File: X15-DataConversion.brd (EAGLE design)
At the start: 24.3 x 25.4 mm, 24 parts, among them Y1 ECS-80-18-30-JGN-TR

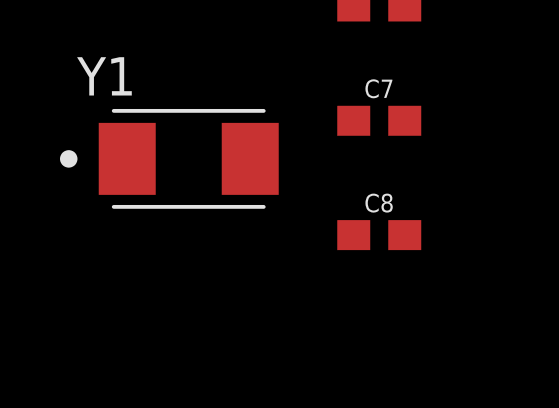
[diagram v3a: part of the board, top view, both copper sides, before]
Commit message: oscillator resistor and capacitor labels
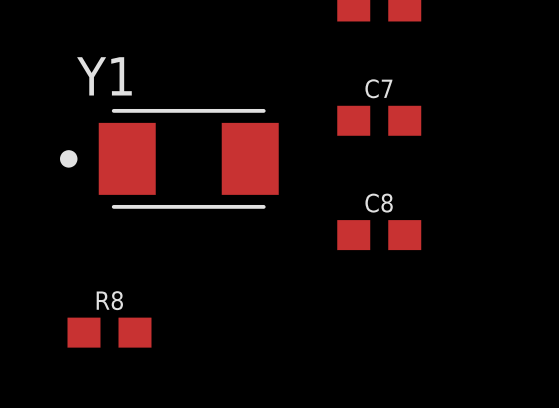
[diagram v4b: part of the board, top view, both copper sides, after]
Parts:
- added R8: 0, SparkFun-Resistors:0603
- R9: value 1.5k -> 0
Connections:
- net OSC_IN: now also R8.1, R8.2
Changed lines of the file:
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@@
 <attribute name="VALUE" x="-36.83" y="-83.312" size="0.6096" layer="27" font="vector" ratio="20" align="top-center"/>
 </element>
-<element name="R9" library="SparkFun-Resistors" package="0603" value="1.5k" x="-36.83" y="-110.49" smashed="yes">
+<element name="R9" library="SparkFun-Resistors" package="0603" value="0" x="-36.83" y="-110.49" smashed="yes">
 <attribute name="NAME" x="-36.83" y="-109.728" size="0.6096" layer="25" font="vector" ratio="20" align="bottom-center"/>
 <attribute name="PROD_ID" value=" " x="-35.56" y="-110.49" size="1.778" layer="27" display="off"/>
@@
 <attribute name="PURCHASE-URL" value="https://pricing.snapeda.com/search/part/ECS-80-18-30-JGN-TR/?ref=eda" x="-43.18" y="-115.57" size="1.778" layer="27" display="off"/>
 <attribute name="VALUE" x="-46.89308125" y="-119.0322" size="1.274490625" layer="27"/>
+</element>
+<element name="R8" library="SparkFun-Resistors" package="0603" value="0" x="-45.8216" y="-121.3612" smashed="yes">
+<attribute name="NAME" x="-45.8216" y="-120.5992" size="0.6096" layer="25" font="vector" ratio="20" align="bottom-center"/>
+<attribute name="PROD_ID" value=" " x="-45.6946" y="-121.3612" size="1.778" layer="27" display="off"/>
+<attribute name="VALUE" x="-45.8216" y="-122.1232" size="0.6096" layer="27" font="vector" ratio="20" align="top-center"/>
 </element>
 </elements>
@@
 <contactref element="C7" pad="1"/>
 <contactref element="Y1" pad="1"/>
+<contactref element="R8" pad="1"/>
+<contactref element="R8" pad="2"/>
+<wire x1="-44.9716" y1="-121.3612" x2="-46.6716" y2="-121.3612" width="0" layer="19" extent="1-1"/>
+<wire x1="-45.23" y1="-115.57" x2="-44.9716" y2="-121.3612" width="0" layer="19" extent="1-1"/>
 <wire x1="-37.68" y1="-114.3" x2="-45.23" y2="-115.57" width="0" layer="19" extent="1-1"/>
 <wire x1="-8.5" y1="-48.36" x2="-37.68" y2="-114.3" width="0" layer="19" extent="1-1"/>

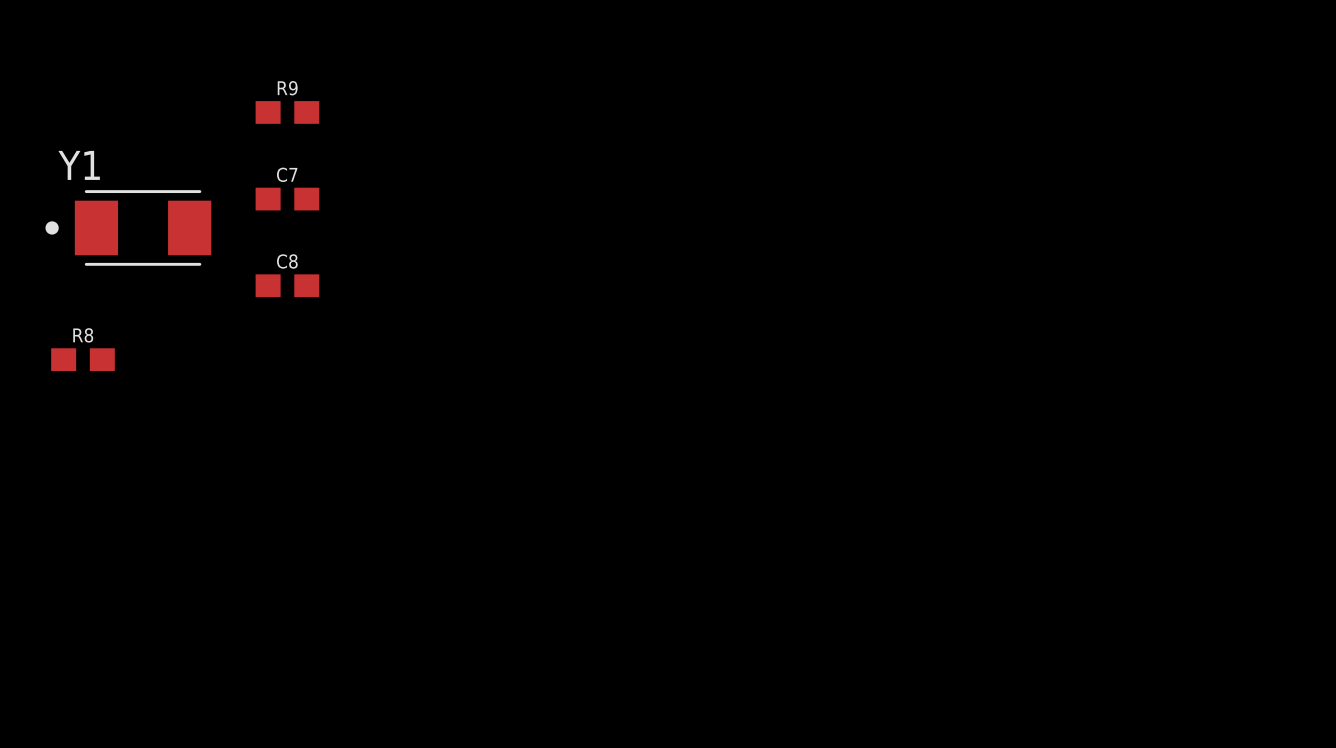
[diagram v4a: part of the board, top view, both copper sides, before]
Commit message: replaced oscillator with same one as on Pi Shield
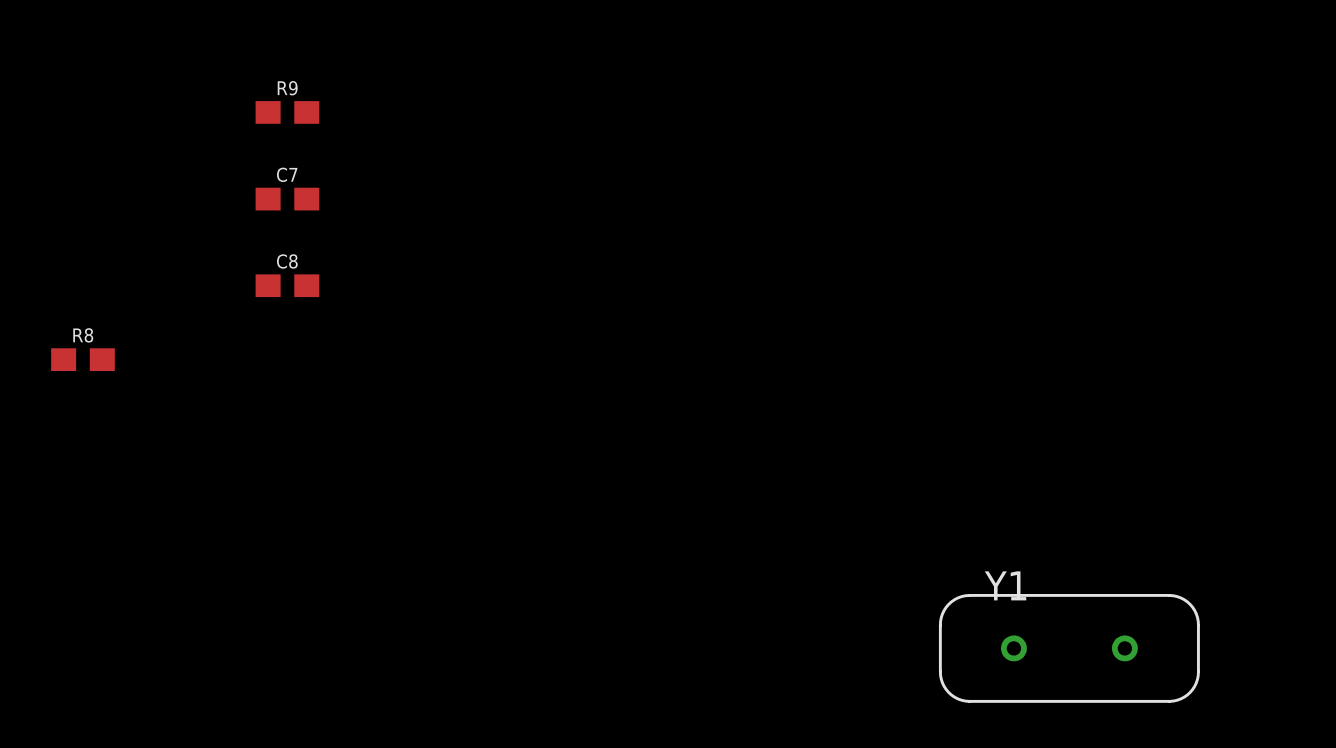
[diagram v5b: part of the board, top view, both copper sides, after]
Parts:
- Y1: value ECS-80-18-30-JGN-TR -> ECS-80-18-4X; device ECS-80-18-30-JGN-TR:XTAL_ECS-80-18-30-JGN-TR -> ECS-80-18-4X:XTAL_ECS-80-18-4X
- moved Y1 44.7 mm to (-2.44, -134.1)
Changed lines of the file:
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@@
 <setting verticaltext="up"/>
 </settings>
-<grid distance="1" unitdist="mil" unit="mil" style="lines" multiple="1" display="no" altdistance="5" altunitdist="mil" altunit="mil"/>
+<grid distance="2" unitdist="mm" unit="mm" style="lines" multiple="1" display="yes" altdistance="5" altunitdist="mil" altunit="mil"/>
 <layers>
 <layer number="1" name="Top" color="4" fill="1" visible="yes" active="yes"/>
@@
 <attribute name="VALUE" x="-36.83" y="-118.872" size="0.6096" layer="27" font="vector" ratio="20" align="top-center"/>
 </element>
-<element name="Y1" library="ECS-80-18-30-JGN-TR" package="XTAL_ECS-80-18-30-JGN-TR" value="ECS-80-18-30-JGN-TR" x="-43.18" y="-115.57" smashed="yes">
-<attribute name="DESCRIPTION" value=" 8 MHz ±20ppm Crystal 18pF 100 Ohms 2-SMD, No Lead " x="-43.18" y="-115.57" size="1.778" layer="27" display="off"/>
-<attribute name="DIGI-KEY_PART_NUMBER" value="XC2103TR-ND" x="-43.18" y="-115.57" size="1.778" layer="27" display="off"/>
-<attribute name="MF" value="ECS Inc." x="-43.18" y="-115.57" size="1.778" layer="27" display="off"/>
-<attribute name="MP" value="ECS-80-18-30-JGN-TR" x="-43.18" y="-115.57" size="1.778" layer="27" display="off"/>
-<attribute name="NAME" x="-46.89928125" y="-113.45771875" size="1.27743125" layer="25"/>
-<attribute name="PACKAGE" value="SMD-2 ECS International" x="-43.18" y="-115.57" size="1.778" layer="27" display="off"/>
-<attribute name="PURCHASE-URL" value="https://pricing.snapeda.com/search/part/ECS-80-18-30-JGN-TR/?ref=eda" x="-43.18" y="-115.57" size="1.778" layer="27" display="off"/>
-<attribute name="VALUE" x="-46.89308125" y="-119.0322" size="1.274490625" layer="27"/>
+<element name="Y1" library="ECS-80-18-4X" package="XTAL_ECS-80-18-4X" value="ECS-80-18-4X" x="-2.44" y="-134.0612" smashed="yes">
+<attribute name="DESCRIPTION" value=" 8 MHz ±30ppm Crystal 18pF 80 Ohms HC-49/US " x="-2.44" y="-134.0612" size="1.778" layer="27" display="off"/>
+<attribute name="DIGI-KEY_PART_NUMBER" value="X1093-ND" x="-2.44" y="-134.0612" size="1.778" layer="27" display="off"/>
+<attribute name="MF" value="ECS Inc." x="-2.44" y="-134.0612" size="1.778" layer="27" display="off"/>
+<attribute name="MP" value="ECS-80-18-4X" x="-2.44" y="-134.0612" size="1.778" layer="27" display="off"/>
+<attribute name="NAME" x="-6.15928125" y="-131.94891875" size="1.27743125" layer="25"/>
+<attribute name="PACKAGE" value="HC-49US ECS Inc." x="-2.44" y="-134.0612" size="1.778" layer="27" display="off"/>
+<attribute name="PURCHASE-URL" value="https://pricing.snapeda.com/search/part/ECS-80-18-4X/?ref=eda" x="-2.44" y="-134.0612" size="1.778" layer="27" display="off"/>
+<attribute name="VALUE" x="-6.15308125" y="-137.5234" size="1.274490625" layer="27"/>
 </element>
 <element name="R8" library="SparkFun-Resistors" package="0603" value="0" x="-45.8216" y="-121.3612" smashed="yes">
@@
 <contactref element="R8" pad="2"/>
 <wire x1="-44.9716" y1="-121.3612" x2="-46.6716" y2="-121.3612" width="0" layer="19" extent="1-1"/>
-<wire x1="-45.23" y1="-115.57" x2="-44.9716" y2="-121.3612" width="0" layer="19" extent="1-1"/>
-<wire x1="-37.68" y1="-114.3" x2="-45.23" y2="-115.57" width="0" layer="19" extent="1-1"/>
+<wire x1="-37.68" y1="-114.3" x2="-44.9716" y2="-121.3612" width="0" layer="19" extent="1-1"/>
+<wire x1="-4.88" y1="-134.0612" x2="-37.68" y2="-114.3" width="0" layer="19" extent="1-1"/>
 <wire x1="-8.5" y1="-48.36" x2="-37.68" y2="-114.3" width="0" layer="19" extent="1-1"/>
 </signal>
@@
 <contactref element="R9" pad="1"/>
 <contactref element="Y1" pad="2"/>
-<wire x1="-37.68" y1="-118.11" x2="-41.13" y2="-115.57" width="0" layer="19" extent="1-1"/>
-<wire x1="-37.68" y1="-110.49" x2="-41.13" y2="-115.57" width="0" layer="19" extent="1-1"/>
+<wire x1="-37.68" y1="-110.49" x2="-37.68" y2="-118.11" width="0" layer="19" extent="1-1"/>
+<wire x1="0" y1="-134.0612" x2="-37.68" y2="-118.11" width="0" layer="19" extent="1-1"/>
 </signal>
 </signals>

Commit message: starting layout
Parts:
- moved U$1 79.8 mm to (8.13, 22.2)
- moved STM 68.8 mm to (10.3, 11.9), turned to 90 degrees

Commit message: starting wiring
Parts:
- Y1: device ECS-80-18-4X:XTAL_ECS-80-18-4X -> OTHER, ECS-80-18-4X:XTAL_ECS-80-18-4X
- moved R8 147.8 mm to (6.80, 16.8)
- moved Y1 144.0 mm to (4.06, 9.81), turned to 90 degrees
- moved R9 136.1 mm to (6.79, 18.4)
- moved C8 133.3 mm to (8.54, 7.26)
- moved C7 127.9 mm to (8.54, 5.33)
- moved CAN_TRANCEIVER 119.7 mm to (18.6, 18.3), turned to 90 degrees
- moved R7 117.3 mm to (20.5, 19.8), flipped to the bottom
- moved R6 115.4 mm to (20.6, 21.4), flipped to the bottom
- moved C6 104.8 mm to (21.9, 11.8)
- moved D3 82.2 mm to (21.8, 7.92), turned to 180 degrees
- moved R5 77.3 mm to (21.8, 10.0), turned to 180 degrees
- moved CONNECTOR1 73.4 mm to (2.16, 2.03)
- moved D1 52.9 mm to (19.0, 8.14), turned to 270 degrees
- moved S1 50.8 mm to (18.6, 2.29), turned to 180 degrees
- moved C3 43.9 mm to (2.77, 17.0), flipped to the bottom, turned to 180 degrees
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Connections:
- removed net N$2: C1.1, R1.1
- new net N$3: C7.1, R8.1, Y1.1
- net NRST: now also C1.1, R1.1
- net OSC_IN: now also R9.2; no longer C7.1, R8.1, R8.2, Y1.1
- net OSC_OUT: now also R8.2; no longer R9.2
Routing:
- net 3.3V: track 0.00 -> 55.5 mm
- net SWDIO: track 0.00 -> 30.5 mm, vias 0 -> 1
- net DATA: track 0.00 -> 18.8 mm
- net CAN_H: track 0.00 -> 17.0 mm, vias 0 -> 1
- net CAN_L: track 0.00 -> 15.6 mm, vias 0 -> 1
- net SWCLK: track 0.00 -> 11.4 mm, vias 0 -> 1
- net NRST: track 0.00 -> 10.8 mm
- net CAN_RX: track 0.00 -> 7.70 mm, vias 0 -> 2
- net ALERT2: track 0.00 -> 7.14 mm
- net OSC_IN: track 0.00 -> 4.63 mm
- net CAN_TX: track 0.00 -> 4.39 mm
- net OSC_OUT: track 0.00 -> 3.82 mm
- net ALERT1: track 0.00 -> 3.15 mm
- net GND: track 0.00 -> 2.83 mm
- net N$1: track 0.00 -> 2.14 mm
- added copper zone on layer 1, net GND
- added copper zone on layer 16, net GND
